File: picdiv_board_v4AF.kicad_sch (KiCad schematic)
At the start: 54 parts, among them J1 DC-Input, J10 PPS_B, J11 PPS_B, J2 MountingHole_M2.5, J3 MountingHole_M2.5, J4 TEST_1PPS, J5 Conn_01x06, J8 PPS_A, J9 PPS_A, SW1 SW_DIP_x03, U1 LT1963AxST-3.3, U2 LT1963AxST-3.3, U3 PIC12F675-xSN, U4 LTC6993xS6-1, U5 IDT5PB1108, U6 IDT5PB1108

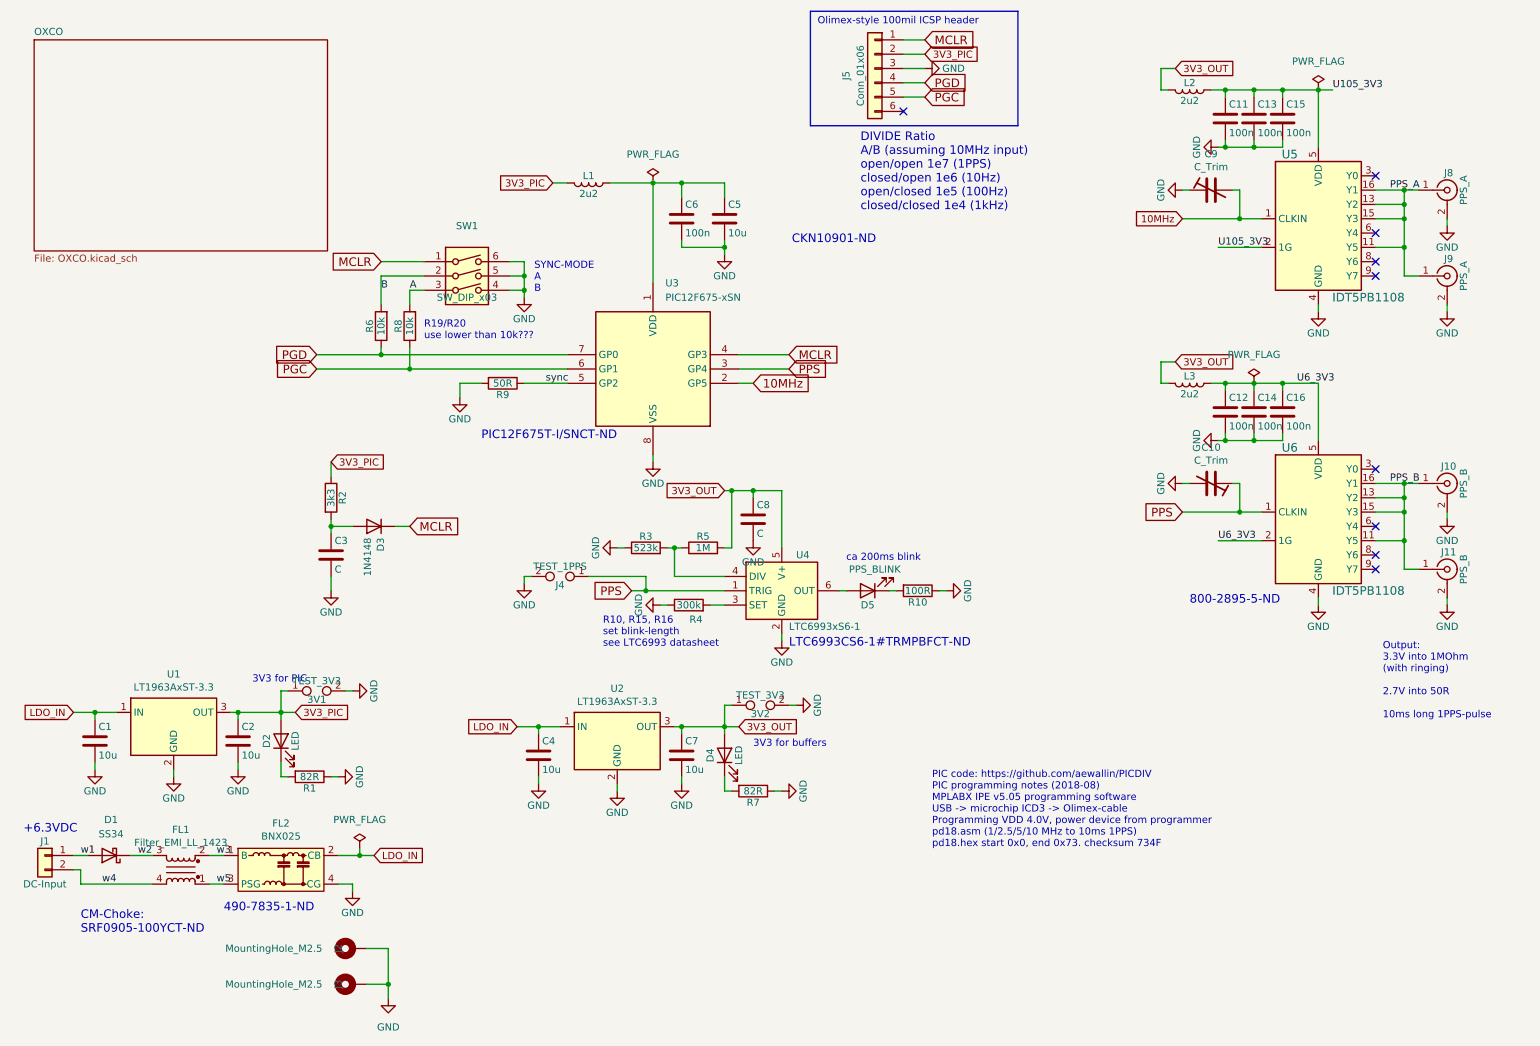
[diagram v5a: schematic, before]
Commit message: Return of sync
Put sync connector back on the schematic.
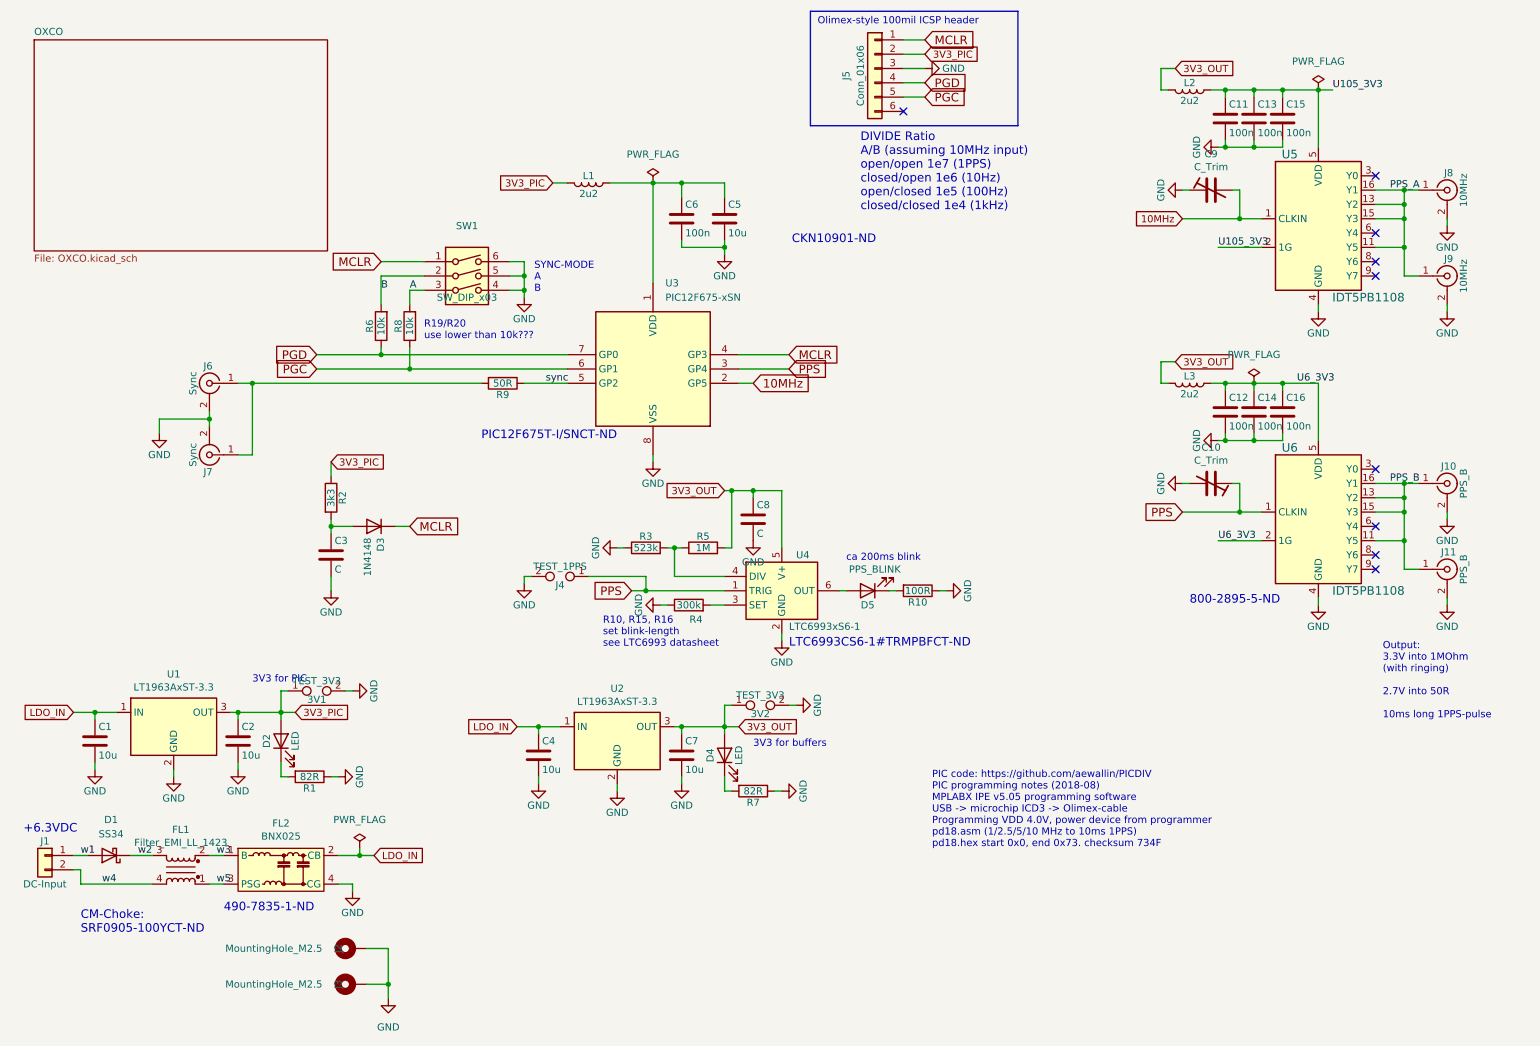
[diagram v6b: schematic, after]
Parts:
- added J6: Sync, Connector_Coaxial:SMA_Molex_73251-2200_Horizontal, symbol Connector:Conn_Coaxial
- added J7: Sync, Connector_Coaxial:BNC_Amphenol_B6252HB-NPP3G-50_Horizontal, symbol Connector:Conn_Coaxial
- J8, J9: value PPS_A -> 10MHz
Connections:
- net GND: now also J6.2 (Ext), J7.2 (Ext); no longer R9.2
- new net: J6.1 (In), J7.1 (In), R9.2
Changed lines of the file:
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@@
 	)
 	(junction
+		(at 57.15 80.01)
+		(diameter 0)
+		(color 0 0 0 0)
+	)
+	(junction
+		(at 49.53 86.36)
+		(diameter 0)
+		(color 0 0 0 0)
+	)
+	(junction
 		(at 234.95 80.01)
 		(diameter 0)
@@
 	(wire
 		(pts
+			(xy 57.15 80.01) (xy 97.79 80.01)
+		)
+		(stroke
+			(width 0)
+			(type default)
+		)
+	)
+	(wire
+		(pts
 			(xy 52.07 168.91) (xy 49.53 168.91)
 		)
@@
 	(wire
 		(pts
+			(xy 49.53 85.09) (xy 49.53 86.36)
+		)
+		(stroke
+			(width 0)
+			(type default)
+		)
+	)
+	(wire
+		(pts
 			(xy 228.6 90.17) (xy 229.87 90.17)
 		)
@@
 		)
 	)
+	(wire
+		(pts
+			(xy 54.61 92.71) (xy 57.15 92.71)
+		)
+		(stroke
+			(width 0)
+			(type default)
+		)
+	)
 	(polyline
 		(pts
@@
 	(wire
 		(pts
+			(xy 54.61 80.01) (xy 57.15 80.01)
+		)
+		(stroke
+			(width 0)
+			(type default)
+		)
+	)
+	(wire
+		(pts
 			(xy 142.24 99.06) (xy 146.05 99.06)
 		)
@@
 	(wire
 		(pts
+			(xy 57.15 80.01) (xy 57.15 92.71)
+		)
+		(stroke
+			(width 0)
+			(type default)
+		)
+	)
+	(wire
+		(pts
 			(xy 261.62 100.33) (xy 261.62 97.79)
 		)
@@
 	(wire
 		(pts
+			(xy 49.53 86.36) (xy 49.53 87.63)
+		)
+		(stroke
+			(width 0)
+			(type default)
+		)
+	)
+	(wire
+		(pts
 			(xy 71.12 105.41) (xy 71.12 106.68)
 		)
@@
 	(wire
 		(pts
-			(xy 236.22 102.87) (xy 232.41 102.87)
+			(xy 40.64 86.36) (xy 40.64 88.9)
 		)
 		(stroke
@@
 	(wire
 		(pts
-			(xy 240.03 80.01) (xy 240.03 81.28)
+			(xy 236.22 102.87) (xy 232.41 102.87)
 		)
 		(stroke
@@
 	(wire
 		(pts
-			(xy 93.98 80.01) (xy 93.98 82.55)
+			(xy 240.03 80.01) (xy 240.03 81.28)
 		)
 		(stroke
@@
 	(wire
 		(pts
+			(xy 49.53 86.36) (xy 40.64 86.36)
+		)
+		(stroke
+			(width 0)
+			(type default)
+		)
+	)
+	(wire
+		(pts
 			(xy 142.24 137.16) (xy 140.97 137.16)
 		)
@@
 	(wire
 		(pts
-			(xy 97.79 80.01) (xy 93.98 80.01)
-		)
-		(stroke
-			(width 0)
-			(type default)
-		)
-	)
-	(wire
-		(pts
 			(xy 236.22 107.95) (xy 228.6 107.95)
 		)
@@
 	(symbol
 		(lib_id "power:GND")
-		(at 93.98 82.55 0)
+		(at 40.64 88.9 0)
 		(unit 1)
 		(exclude_from_sim no)
@@
 		(dnp no)
 		(property "Reference" "#PWR021"
-			(at 93.98 88.9 0)
+			(at 40.64 95.25 0)
 			(effects
 				(font
@@
 		)
 		(property "Value" "GND"
-			(at 93.98 86.36 0)
+			(at 40.64 92.71 0)
 			(effects
 				(font
@@
 		)
 		(property "Footprint" ""
-			(at 93.98 82.55 0)
+			(at 40.64 88.9 0)
 			(effects
 				(font
@@
 		)
 		(property "Datasheet" ""
-			(at 93.98 82.55 0)
+			(at 40.64 88.9 0)
 			(effects
 				(font
@@
 		)
 		(property "Description" "Power symbol creates a global label with name \"GND\" , ground"
-			(at 93.98 82.55 0)
+			(at 40.64 88.9 0)
 			(effects
 				(font
@@
 			)
 		)
-		(property "Value" "PPS_A"
+		(property "Value" "10MHz"
 			(at 272.161 60.96 90)
 			(effects
@@
 			)
 		)
-		(property "Value" "PPS_A"
+		(property "Value" "10MHz"
 			(at 272.161 45.72 90)
 			(effects
@@
 	)
 	(symbol
+		(lib_id "Connector:Conn_Coaxial")
+		(at 49.53 92.71 180)
+		(unit 1)
+		(exclude_from_sim yes)
+		(in_bom yes)
+		(on_board yes)
+		(dnp no)
+		(property "Reference" "J7"
+			(at 49.276 95.758 0)
+			(effects
+				(font
+					(size 1.27 1.27)
+				)
+			)
+		)
+		(property "Value" "Sync"
+			(at 46.609 92.71 90)
+			(effects
+				(font
+					(size 1.27 1.27)
+				)
+			)
+		)
+		(property "Footprint" "Connector_Coaxial:BNC_Amphenol_B6252HB-NPP3G-50_Horizontal"
+			(at 49.53 92.71 0)
+			(effects
+				(font
+					(size 1.27 1.27)
+				)
+				(hide yes)
+			)
+		)
+		(property "Datasheet" "~"
+			(at 49.53 92.71 0)
+			(effects
+				(font
+					(size 1.27 1.27)
+				)
+				(hide yes)
+			)
+		)
+		(property "Description" "coaxial connector (BNC, SMA, SMB, SMC, Cinch/RCA, LEMO, ...)"
+			(at 49.53 92.71 0)
+			(effects
+				(font
+					(size 1.27 1.27)
+				)
+				(hide yes)
+			)
+		)
+		(pin "1"
+		)
+		(pin "2"
+		)
+		(instances
+			(project "picdiv_board_v4AF"
+				(path "/eba36321-b5f3-4bd6-a805-57b9b2ee447e"
+					(reference "J7")
+					(unit 1)
+				)
+			)
+		)
+	)
+	(symbol
 		(lib_id "power:PWR_FLAG")
 		(at 246.38 27.94 0)
@@
 					(unit 1)
 				)
+			)
+		)
+	)
+	(symbol
+		(lib_id "Connector:Conn_Coaxial")
+		(at 49.53 80.01 0)
+		(mirror y)
+		(unit 1)
+		(exclude_from_sim yes)
+		(in_bom yes)
+		(on_board yes)
+		(dnp no)
+		(property "Reference" "J6"
+			(at 49.276 76.962 0)
+			(effects
+				(font
+					(size 1.27 1.27)
+				)
+			)
+		)
+		(property "Value" "Sync"
+			(at 46.609 80.01 90)
+			(effects
+				(font
+					(size 1.27 1.27)
+				)
+			)
+		)
+		(property "Footprint" "Connector_Coaxial:SMA_Molex_73251-2200_Horizontal"
+			(at 49.53 80.01 0)
+			(effects
+				(font
+					(size 1.27 1.27)
+				)
+				(hide yes)
+			)
+		)
+		(property "Datasheet" "~"
+			(at 49.53 80.01 0)
+			(effects
+				(font
+					(size 1.27 1.27)
+				)
+				(hide yes)
+			)
+		)
+		(property "Description" "coaxial connector (BNC, SMA, SMB, SMC, Cinch/RCA, LEMO, ...)"
+			(at 49.53 80.01 0)
+			(effects
+				(font
+					(size 1.27 1.27)
+				)
+				(hide yes)
+			)
+		)
+		(pin "1"
+		)
+		(pin "2"
+		)
+		(instances
+			(project "picdiv_board_v4AF"
+				(path "/eba36321-b5f3-4bd6-a805-57b9b2ee447e"
+					(reference "J6")
+					(unit 1)
+				)

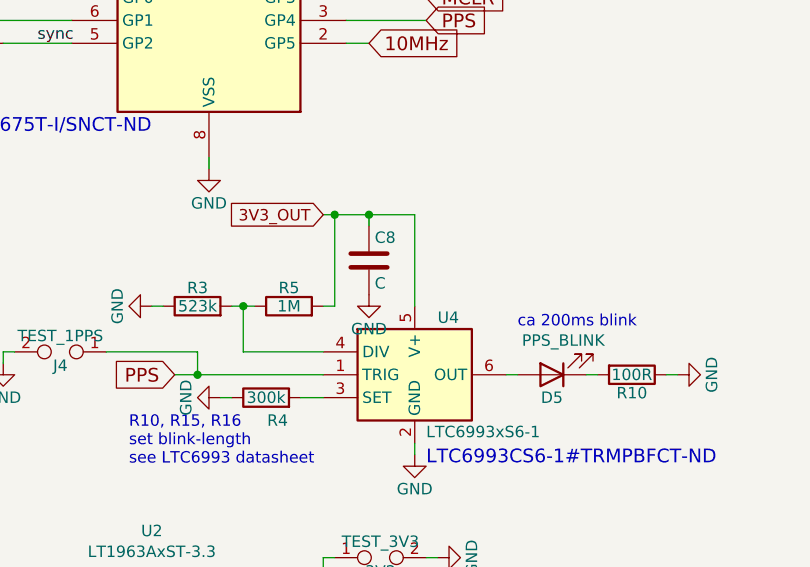
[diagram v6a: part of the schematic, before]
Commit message: More layout work
99.5x100 mm board.
Sync back on the schematic.
Move some parts to make room for OCXO
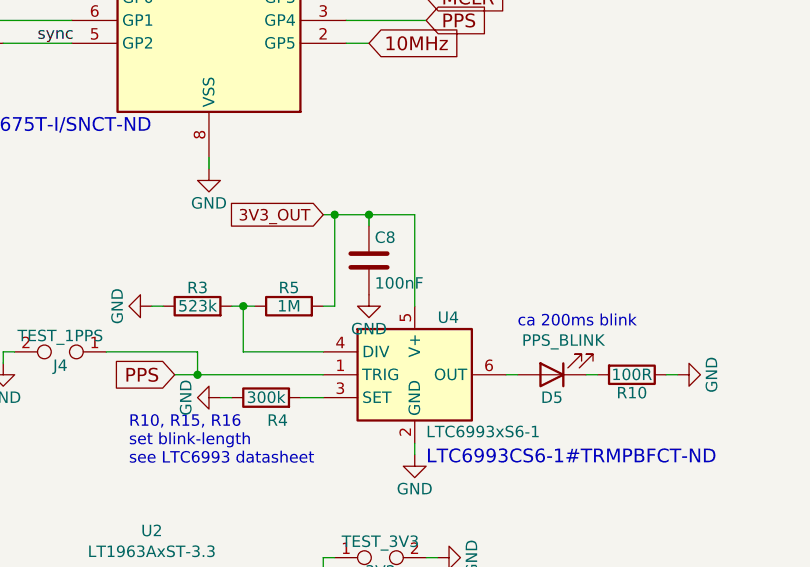
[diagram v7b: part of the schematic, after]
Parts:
- C8: value C -> 100nF; LCSC (none) -> C49678; MPN (none) -> CC0805KRX7R9BB104
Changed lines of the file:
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@@
 			)
 		)
-		(property "Value" "C"
+		(property "Value" "100nF"
 			(at 146.685 106.68 0)
 			(effects
@@
 			(at 146.05 104.14 0)
 			(effects
+				(font
+					(size 1.27 1.27)
+				)
+				(hide yes)
+			)
+		)
+		(property "MPN" "CC0805KRX7R9BB104"
+			(at 146.05 104.14 0)
+			(effects
+				(font
+					(size 1.27 1.27)
+				)
+				(hide yes)
+			)
+		)
+		(property "LCSC" "C49678"
+			(at 146.05 104.14 0)
+			(effects

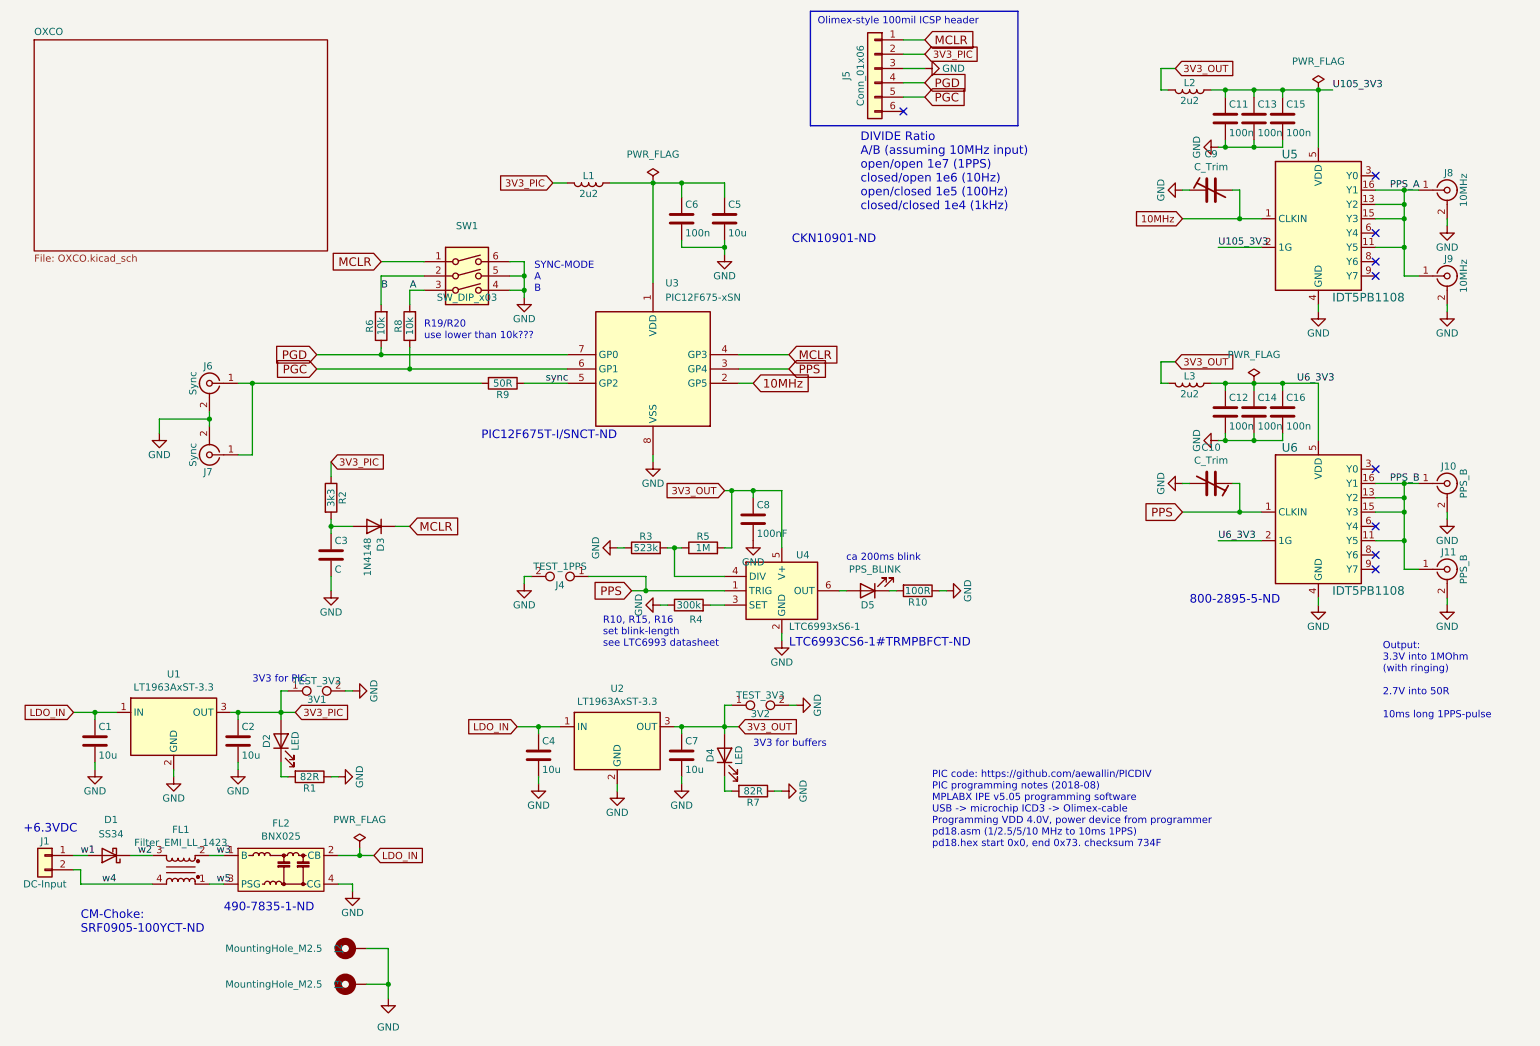
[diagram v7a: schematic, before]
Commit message: More Layout work
All parts are "on the board".    Added some missing LCSC part numbers.  Fixed a few "lost parts" that happened when I updated the original schematic to the current version of KiCad.
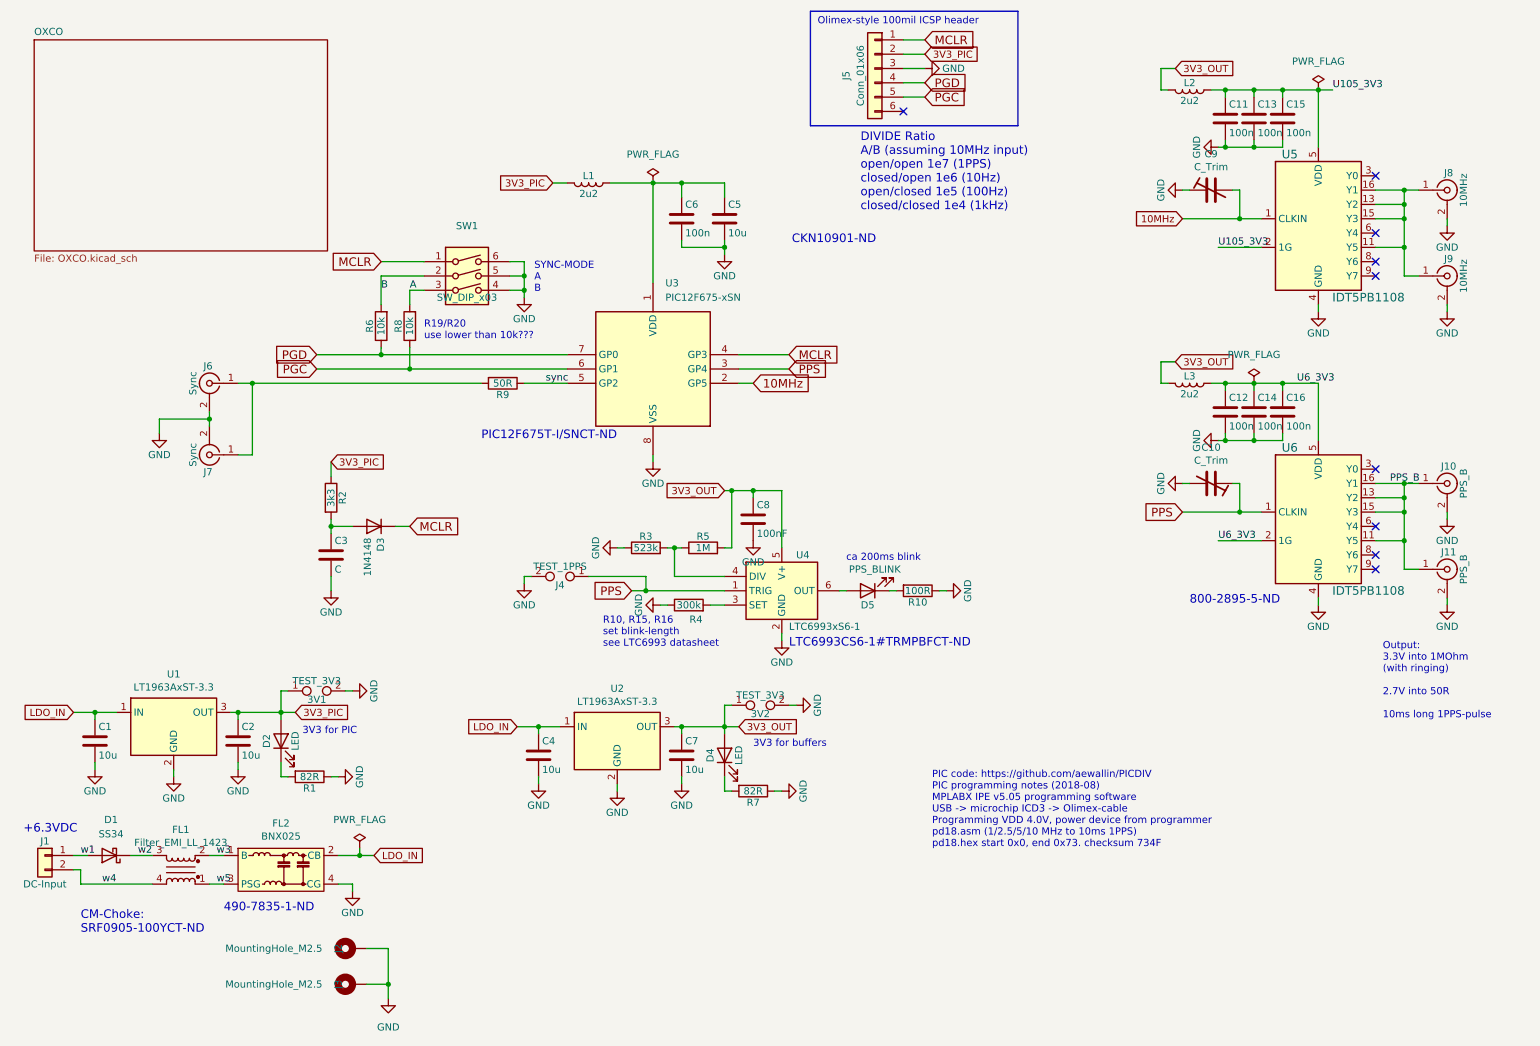
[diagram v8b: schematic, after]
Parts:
- R6, R8: LCSC (none) -> C17414; MPN (none) -> 0805W8F1002T5E
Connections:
- net PPS_A: no longer names the net of J8.1 (In), J9.1 (In), U5.11 (Y5), U5.13 (Y2), U5.15 (Y3), U5.16 (Y1)
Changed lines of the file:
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@@
 	(text "3V3 for PIC"
 		(exclude_from_sim no)
-		(at 57.15 133.35 0)
+		(at 66.04 142.494 0)
 		(effects
 			(font
@@
 		)
 	)
-	(label "PPS_A"
-		(at 259.08 45.72 0)
-		(fields_autoplaced yes)
-		(effects
-			(font
-				(size 1.27 1.27)
-			)
-			(justify left bottom)
-		)
-	)
 	(label "w4"
 		(at 30.48 168.91 0)
@@
 			)
 		)
+		(property "MPN" "0805W8F1002T5E"
+			(at 80.01 69.85 90)
+			(effects
+				(font
+					(size 1.27 1.27)
+				)
+				(hide yes)
+			)
+		)
+		(property "LCSC" "C17414"
+			(at 80.01 69.85 90)
+			(effects
+				(font
+					(size 1.27 1.27)
+				)
+				(hide yes)
+			)
+		)
 		(pin "1"
 		)
@@
 			(effects
 				(font
+					(size 1.27 1.27)
+				)
+				(hide yes)
+			)
+		)
+		(property "MPN" "0805W8F1002T5E"
+			(at 85.09 69.85 90)
+			(effects
+				(font
+					(size 1.27 1.27)
+				)
+				(hide yes)
+			)
+		)
+		(property "LCSC" "C17414"
+			(at 85.09 69.85 90)
+			(effects
+				(font
